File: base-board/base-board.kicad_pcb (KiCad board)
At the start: 2 copper layers, 49.8 x 49.8 mm, 6 parts, among them J1 Barrel_Jack_MountingPin, J2 Conn_01x01_Female

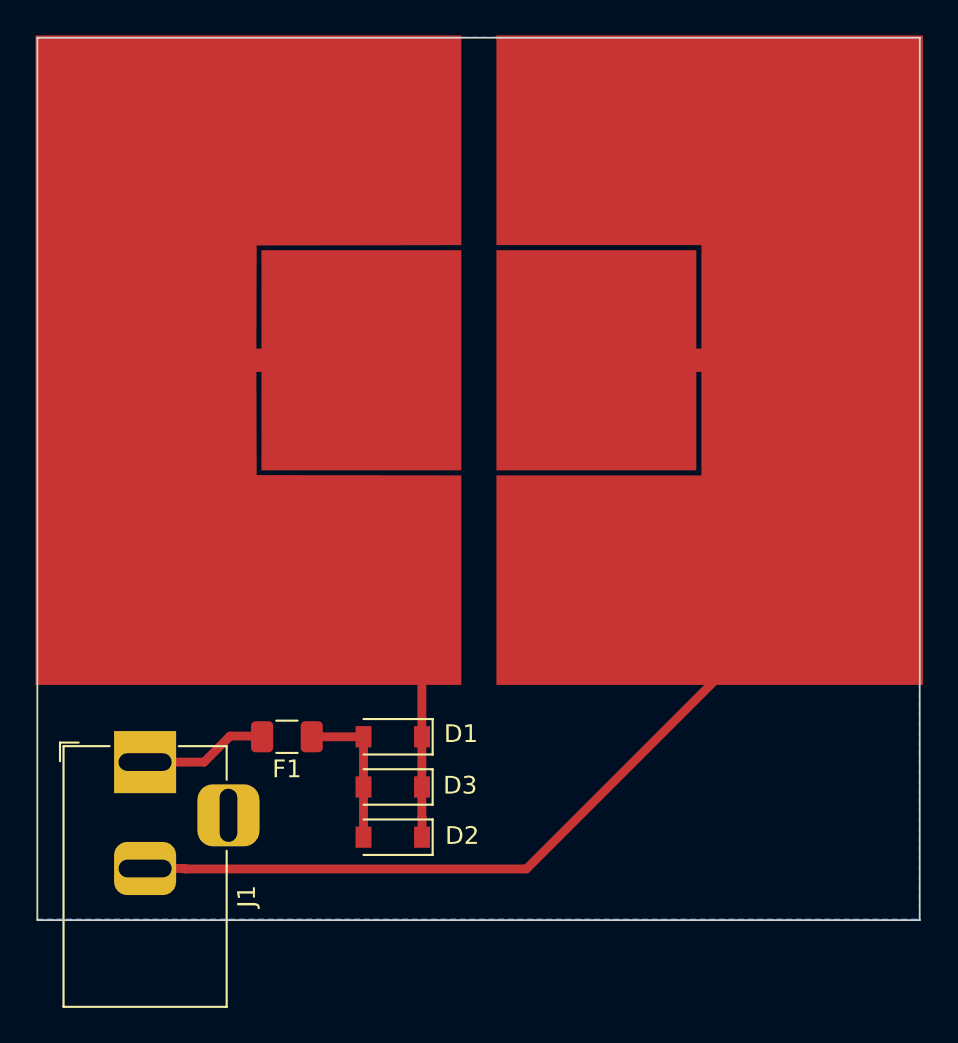
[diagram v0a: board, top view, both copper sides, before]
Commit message: Switch to surface mount barrel jack
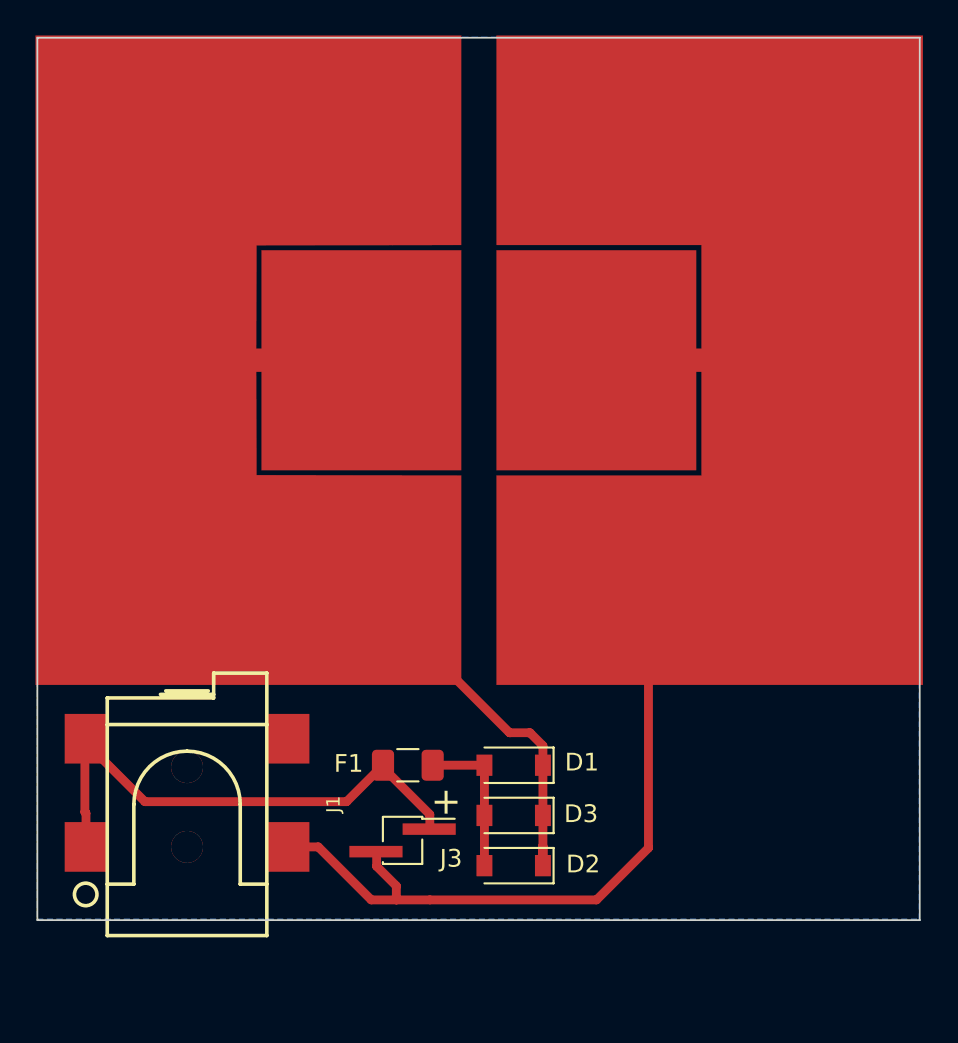
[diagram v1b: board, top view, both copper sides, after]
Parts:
- added J3: Conn_01x02_Male, KiCad/kicad-footprints/Connector_PinHeader_1.27mm.pretty:PinHeader_1x02_P1.27mm_Vertical_SMD_Pin1Right, F.Cu at (159.7, 118.4)
- J1: footprint KiCad/kicad-footprints/Connector_BarrelJack.pretty:BarrelJack_Horizontal -> mcous/kicad-lib/footprints/connect-sm.pretty:CUI-PJ-002AH-SMT_dc-barrel-jack
- moved D2 7.00 mm to (165.9, 119.8)
- moved D3 7.00 mm to (165.9, 117.0)
- moved D1 7.00 mm to (165.9, 114.1)
- moved F1 7.00 mm to (160.0, 114.1)
- moved J1 3.36 mm to (147.5, 116.3)
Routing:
- net Net-(F1-Pad2): track 9.03 -> 29.9 mm
- net -: track 46.5 -> 37.2 mm
- net +: track 13.1 -> 14.9 mm
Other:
- board text added: "+"
